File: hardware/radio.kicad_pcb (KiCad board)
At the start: 4 copper layers, 65 x 56 mm, 89 parts, among them J1 JCLK, U1 G144A12, U3V3t1V8 NCP1117ST18T3G, U5V0t3V3 NCP1117ST33T3G

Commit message: Getting close to first production run.
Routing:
- net GND: track 412.5 -> 334.1 mm
- net VDD: track 224.3 -> 203.3 mm

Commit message: Small adjustments from doing paper fit.
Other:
- board text added: "G O G I V O G I G"
- board text added: "V O G I G"

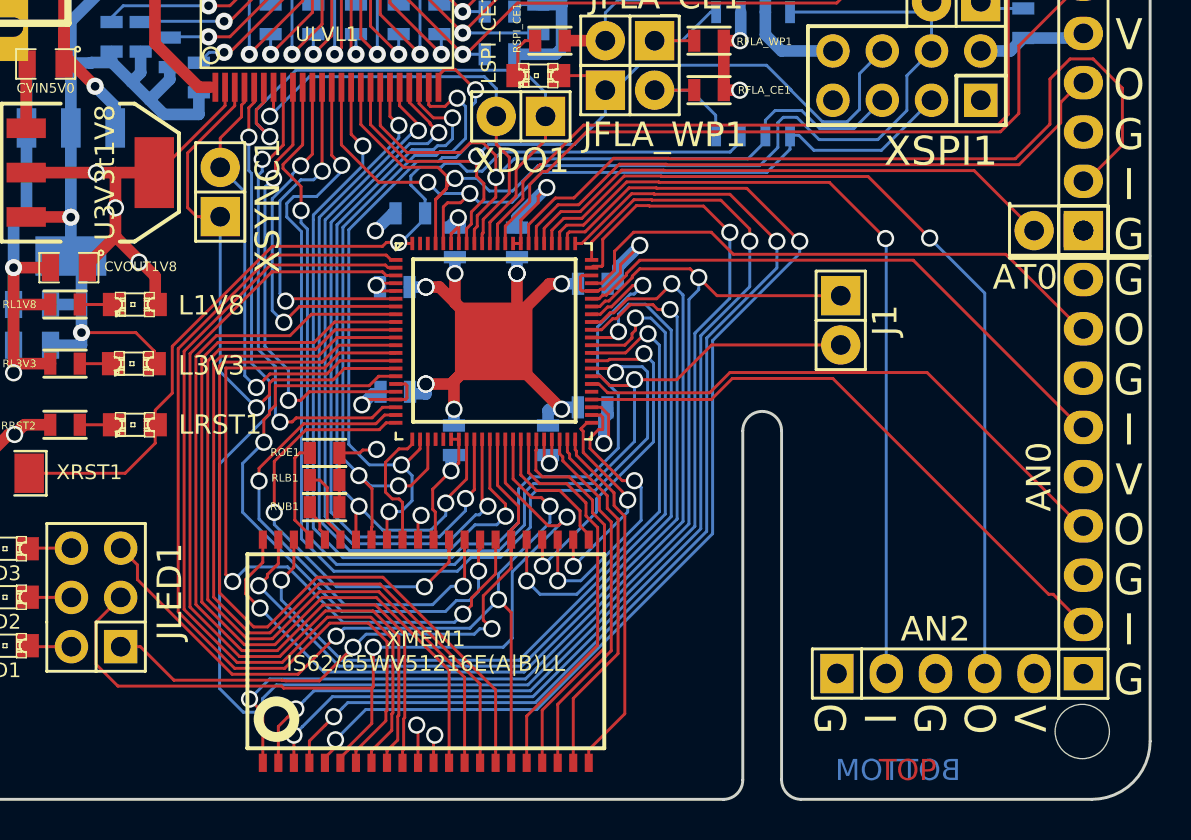
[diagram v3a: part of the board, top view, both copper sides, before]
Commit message: Extending the solder pads for the RAM chip.
Fixes #3.
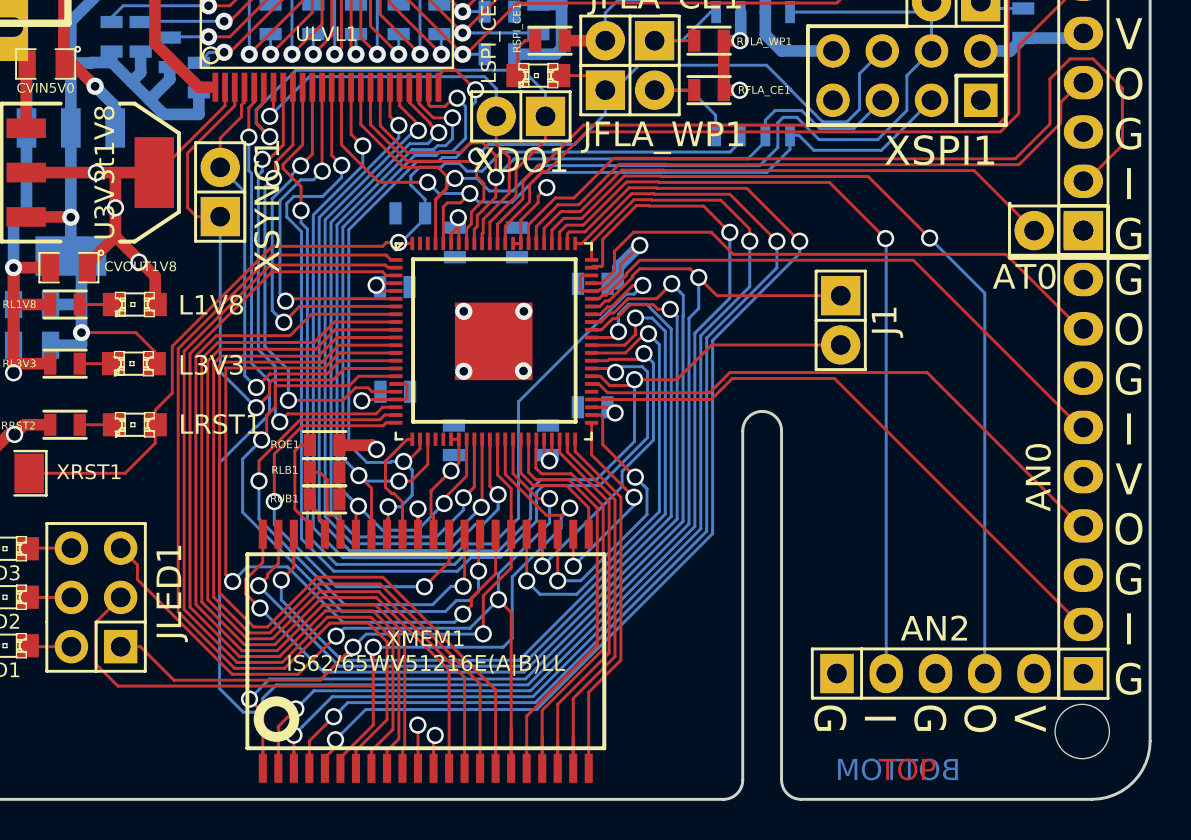
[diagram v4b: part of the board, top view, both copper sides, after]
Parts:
- moved ROE1 0.40 mm to (39.4, 55.0)
- moved RLB1 0.40 mm to (39.4, 56.5)
- moved RUB1 0.40 mm to (39.4, 57.9)
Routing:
- net GND: track 334.1 -> 297.0 mm, vias 20 -> 14
- net VDD: track 203.3 -> 192.4 mm, vias 15 -> 14
- net /GPIO_25_L: track 56.9 -> 54.2 mm
- net /~WE: track 43.3 -> 45.3 mm
- net /ADDR15: track 20.3 -> 21.9 mm
- net /ADDR13: track 18.7 -> 20.2 mm
- net /ADDR3: track 53.3 -> 54.8 mm
- net /ADDR14: track 18.9 -> 20.4 mm
- net /ADDRN18: track 32.7 -> 31.3 mm
- net /ADDR16: track 20.5 -> 21.8 mm
- net /ADDR7: track 42.1 -> 43.4 mm
- net /ADDR6: track 44.5 -> 45.4 mm
- net /ADDR4: track 47.2 -> 48.1 mm
- net /ADDR2: track 53.9 -> 54.7 mm
- net /ADDR10: track 15.5 -> 14.7 mm
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
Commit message: Fixing some vias.
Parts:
- turned RRST1 to 180 degrees
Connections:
- U3V3t1V8 pad 4: (no net) -> VDD
- U5V0t3V3 pad 4: (no net) -> +3.3V
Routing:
- net VDD: track 192.4 -> 200.0 mm
- net GND: track 297.0 -> 303.2 mm, vias 14 -> 22
- net RST: track 49.9 -> 50.7 mm

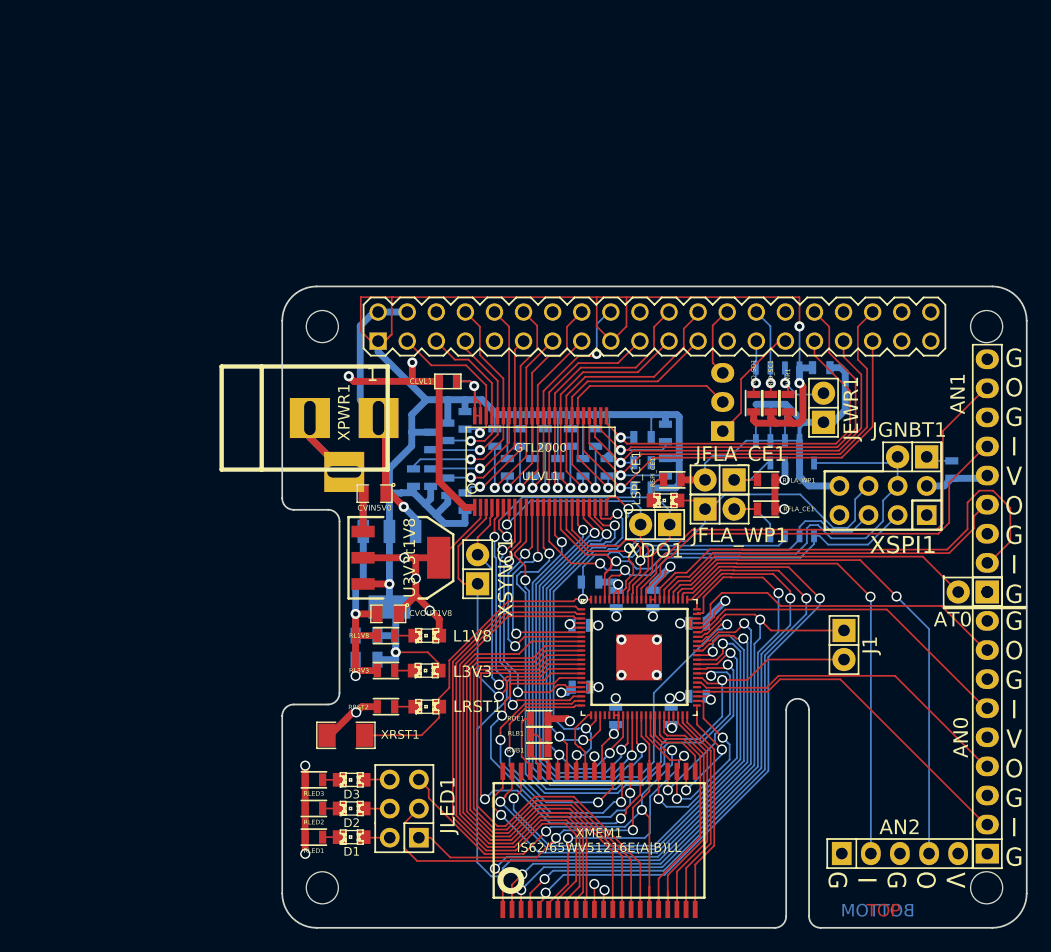
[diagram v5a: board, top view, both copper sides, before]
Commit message: Routing update.
Also makes a huge pad for adding reset switches onto.

Fixes #5 and #6.
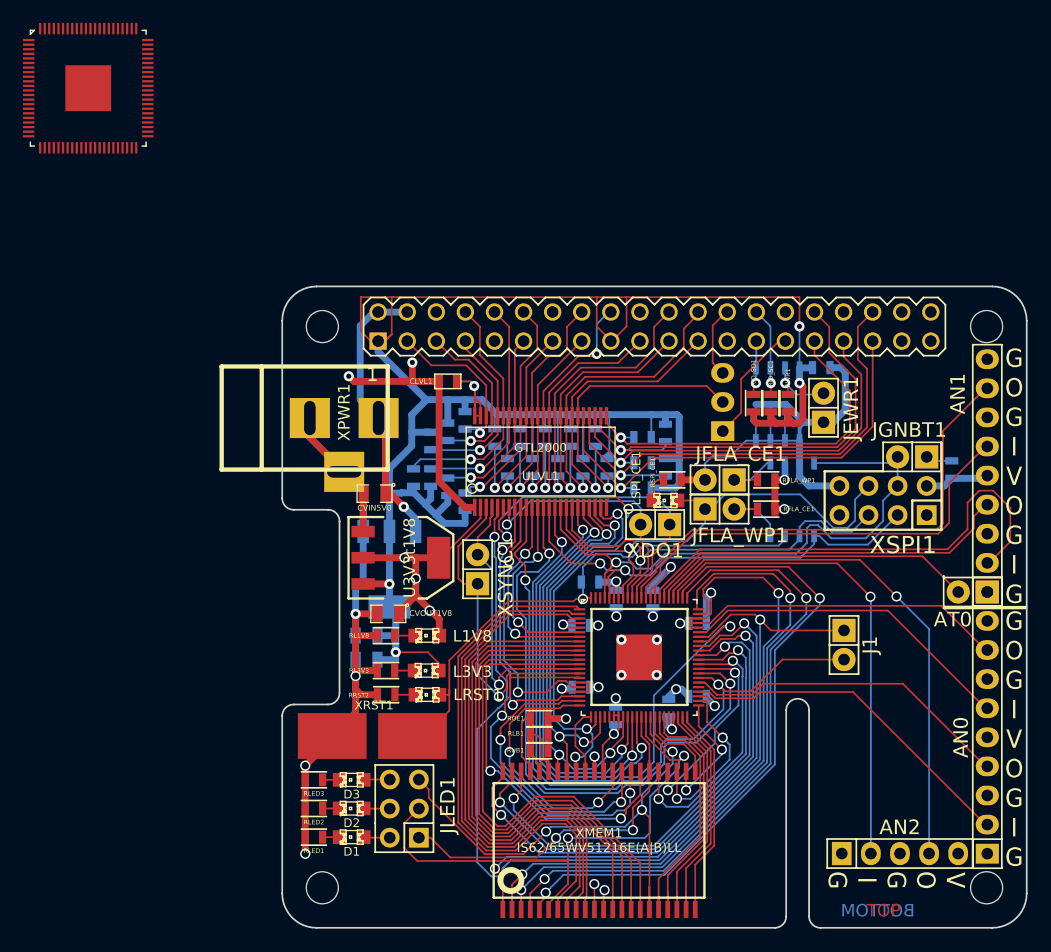
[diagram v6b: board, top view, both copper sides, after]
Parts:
- added U1: G144A12, qfn88:qfn88, F.Cu at (0.00, 0.00)
- moved XRST1 2.31 mm to (24.8, 56.6)
- moved LRST1 1.04 mm to (29.6, 53.0)
- moved RRST2 1.04 mm to (26.0, 53.0)
- moved C6 0.71 mm to (50.7, 54.1)
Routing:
- net GND: track 303.2 -> 311.2 mm, vias 22 -> 20
- net /DATA8: track 38.3 -> 35.1 mm
- net RST: track 50.7 -> 47.8 mm
- net VDD: track 200.0 -> 202.1 mm
- net /617.ao: track 29.1 -> 27.6 mm
- net /GPIO_23_L: track 19.3 -> 17.9 mm
- net /GPIO_24_L: track 54.7 -> 53.7 mm
- net /GPIO_22_L: track 18.2 -> 17.2 mm
- net /ADDR3: track 54.8 -> 55.6 mm
- net /ADDR7: track 43.4 -> 42.6 mm
- net /117.ai: track 31.1 -> 30.5 mm
- net /DATA5: track 44.3 -> 43.7 mm
- net /DATA6: track 44.0 -> 43.5 mm
- net /DATA4: track 44.6 -> 44.1 mm
- net /DATA7: track 43.7 -> 43.1 mm
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
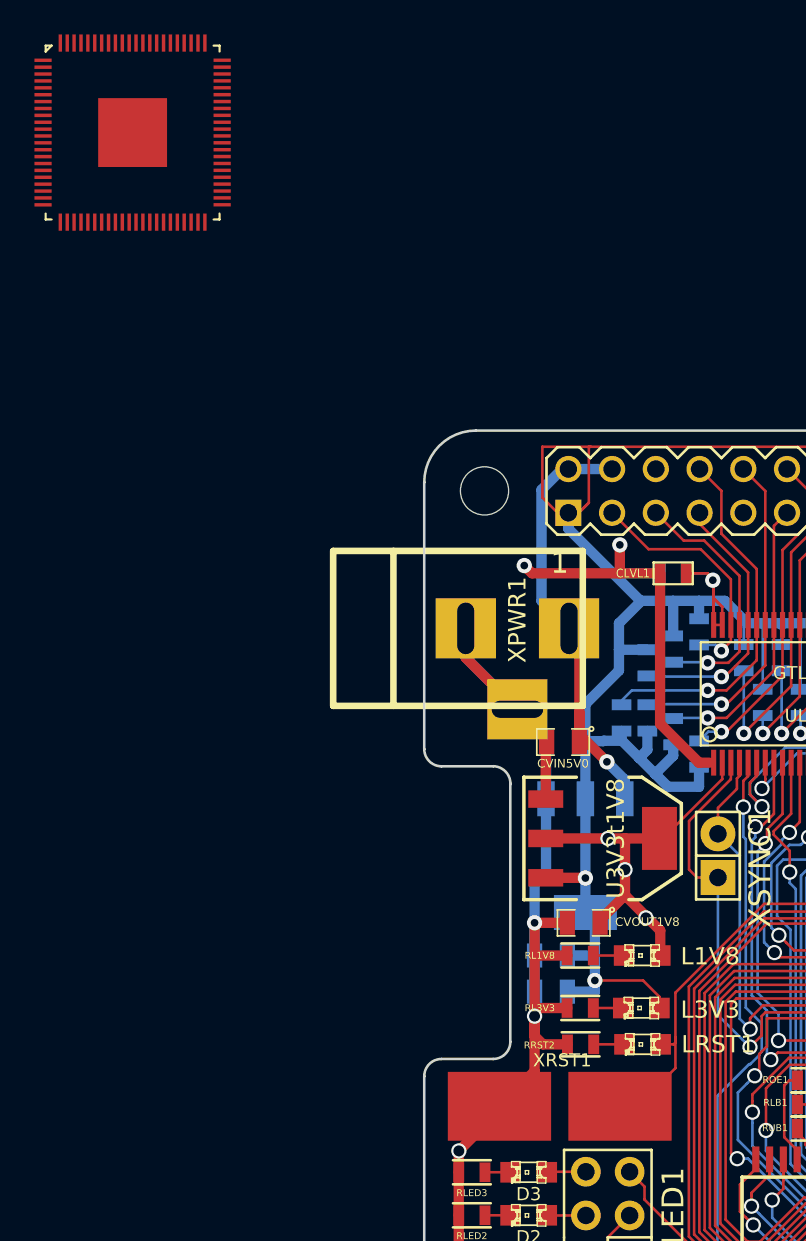
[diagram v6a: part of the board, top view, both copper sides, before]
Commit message: Small silkscreen updates.
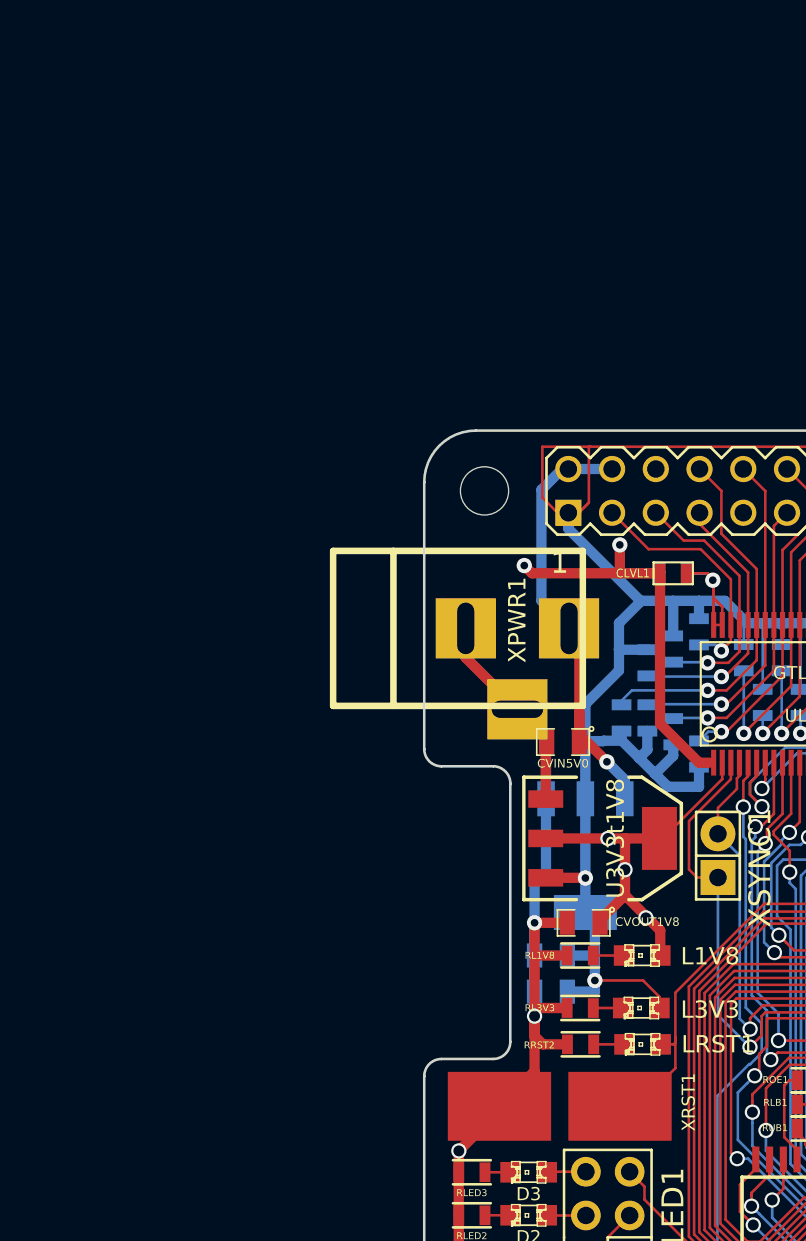
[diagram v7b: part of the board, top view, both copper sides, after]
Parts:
- removed the U1 at (0.00, 0.00)

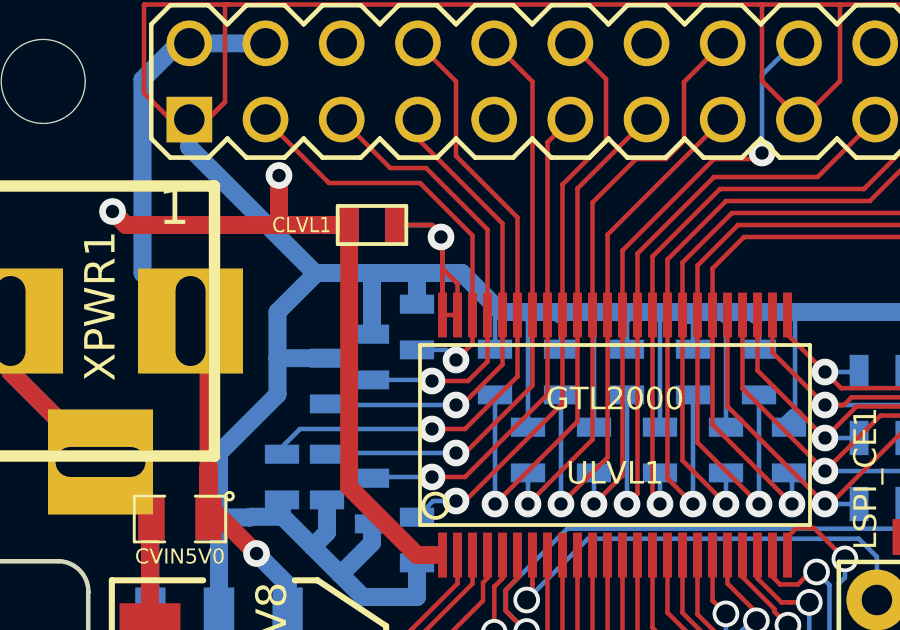
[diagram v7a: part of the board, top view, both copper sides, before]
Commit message: Fixing short on level shifter in top right hand corner.
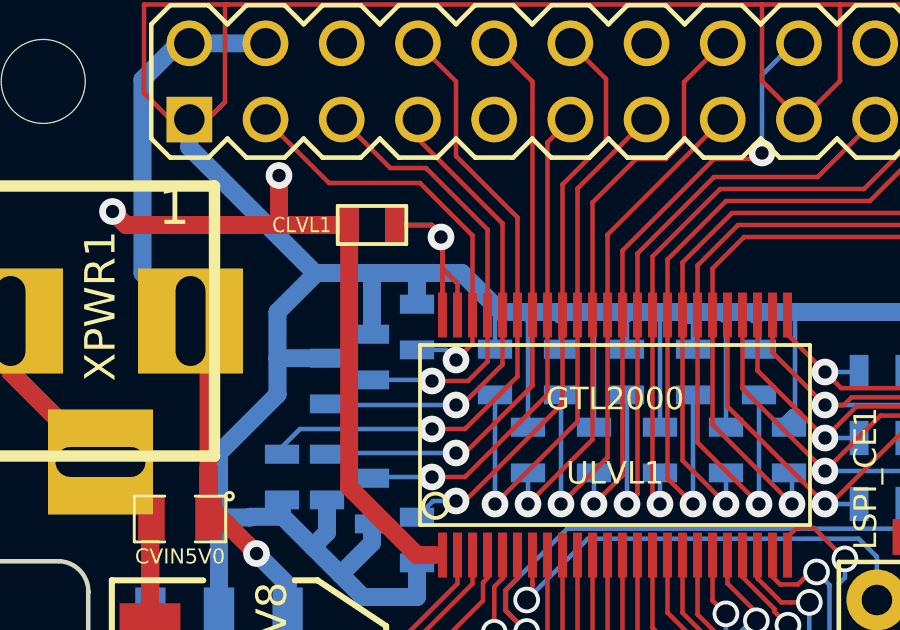
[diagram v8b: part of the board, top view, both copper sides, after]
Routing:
- net Net-(CLVL1-Pad2): track 11.7 -> 11.2 mm
